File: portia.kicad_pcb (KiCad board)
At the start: 2 copper layers, 65.1 x 56.1 mm, 60 parts, among them J1 USB_B_Micro, J11 Conn_01x02, J12 Conn_01x02, J13 Conn_01x02, J14 Conn_01x02, J2 Conn_02x04_Counter_Clockwise, J3 Conn_01x02, J4 Conn_01x02, J5 RASPBERRYPI-40-PIN-GPIO, J7 Conn_01x02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

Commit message: modified trace connections
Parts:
- removed D8: D, Diode_SMD:D_SOD-123F
- removed JP8, JP9: SolderJumper_2_Open, Jumper:SolderJumper-2_P1.3mm_Open_RoundedPad1.0x1.5mm
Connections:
- J5 pad 1: Net-(D8-Pad1) -> +3V3
- J5 pad 17: Net-(D8-Pad1) -> +3V3
- R15 pad 2: Net-(JP8-Pad2) -> /id_clk
- R16 pad 2: Net-(JP9-Pad2) -> /id_sda
- U6 pad 17: Net-(JP9-Pad2) -> Net-(U6-Pad17)
- U6 pad 18: Net-(JP8-Pad2) -> Net-(U6-Pad18)
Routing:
- net Net-(JP9-Pad2): track 16.3 -> 0.00 mm
- net Net-(D8-Pad1): track 5.24 -> 0.00 mm
- net +5V: track 17.5 -> 12.5 mm
- net /id_sda: track 17.0 -> 21.4 mm
- net +3V3: track 16.8 -> 12.6 mm, vias 2 -> 1
- net GND: track 58.8 -> 54.8 mm, vias 27 -> 26
- net Net-(JP8-Pad2): track 3.46 -> 0.00 mm
- net Net-(F1-Pad1): track 19.7 -> 17.1 mm, vias 3 -> 2
- net /id_clk: track 22.4 -> 23.9 mm
- net Net-(D1-Pad1): track 15.0 -> 15.9 mm
- net Net-(J11-Pad2): track 20.7 -> 20.1 mm

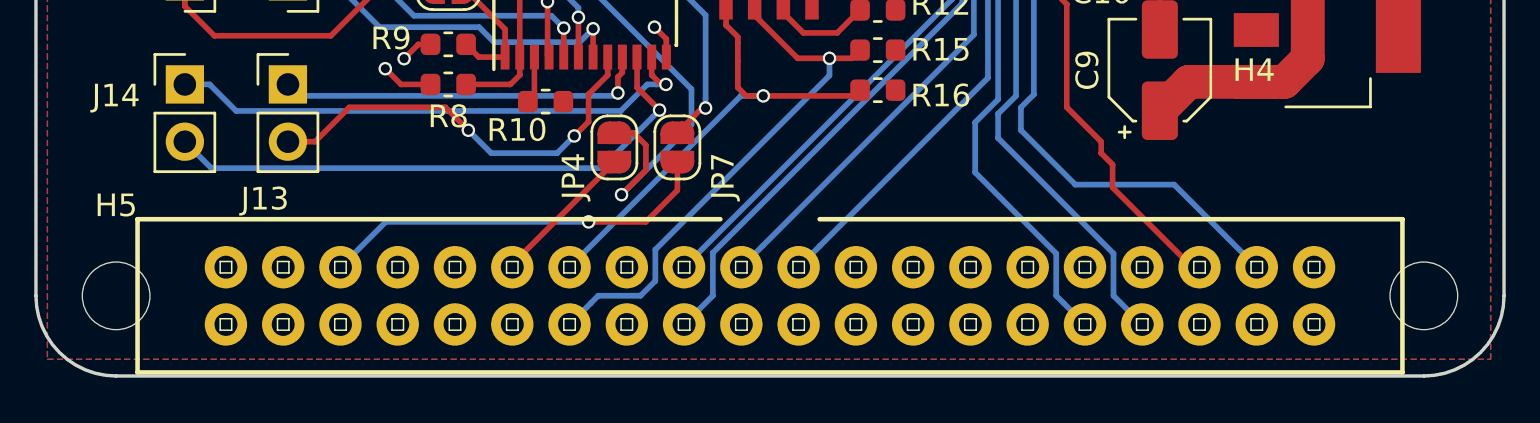
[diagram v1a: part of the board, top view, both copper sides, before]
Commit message: resolved routing issue
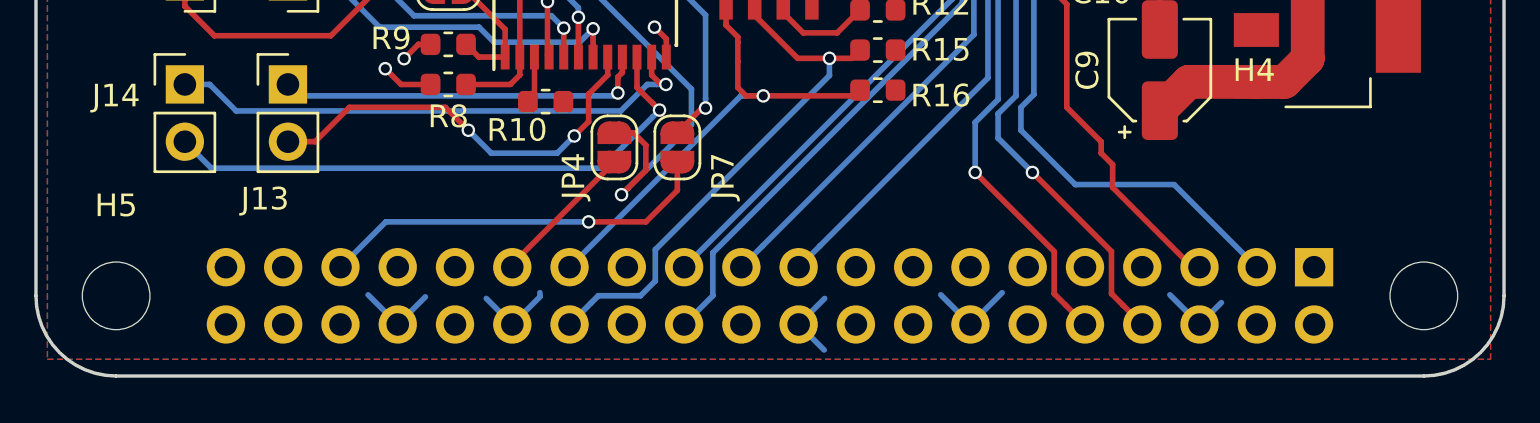
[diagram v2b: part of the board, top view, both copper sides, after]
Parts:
- J5: footprint SparkFun-Boards:2X20-SHROUDED -> Connector_PinSocket_2.54mm:PinSocket_2x20_P2.54mm_Vertical; moved to B.Cu
- moved J5 24.2 mm to (213.2, 129.0), turned to 90 degrees
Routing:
- net GND: track 54.8 -> 72.2 mm
- net /tx: vias 1 -> 2
- net /rx: vias 1 -> 2

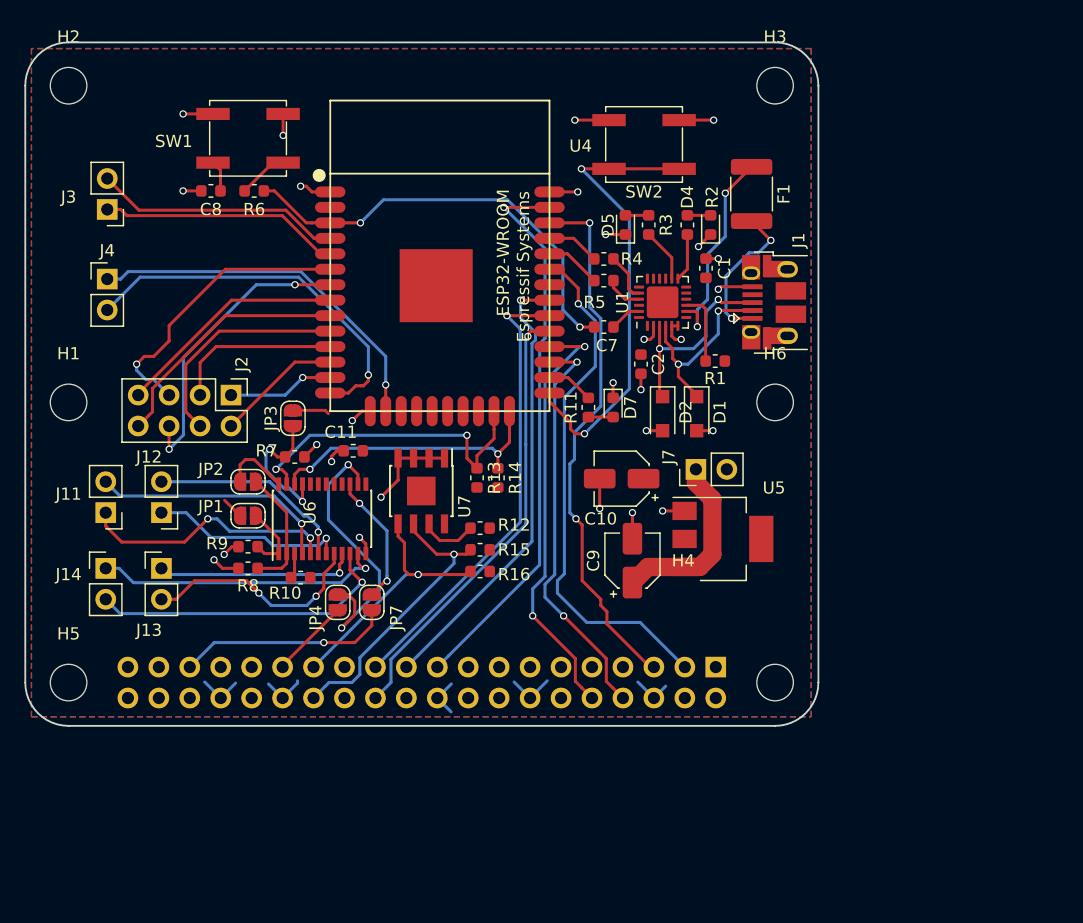
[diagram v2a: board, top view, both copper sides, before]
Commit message: redesign removed 40 pin header
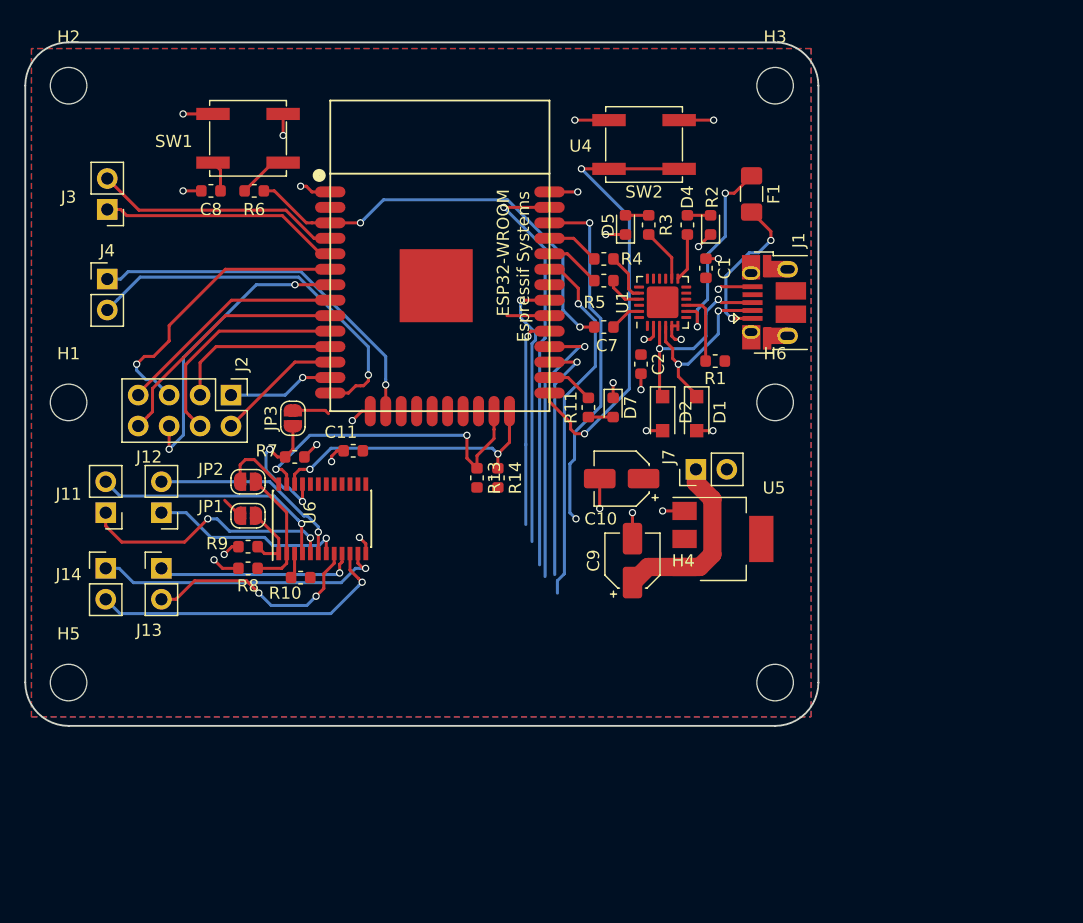
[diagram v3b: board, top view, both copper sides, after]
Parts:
- removed J5: RASPBERRYPI-40-PIN-GPIO, Connector_PinSocket_2.54mm:PinSocket_2x20_P2.54mm_Vertical
- removed JP4, JP7: SolderJumper_2_Open, Jumper:SolderJumper-2_P1.3mm_Open_RoundedPad1.0x1.5mm
- removed R12, R15, R16: R_Small, Resistor_SMD:R_0603_1608Metric
- removed U7: CAT24C256, Package_SO:SOIC-8-1EP_3.9x4.9mm_P1.27mm_EP2.35x2.35mm
- F1: footprint Fuse:Fuse_1812_4532Metric_Pad1.30x3.40mm_HandSolder -> Fuse:Fuse_1206_3216Metric_Pad1.42x1.75mm_HandSolder
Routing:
- net /clk: track 37.7 -> 3.50 mm, vias 1 -> 0
- net GND: track 72.2 -> 47.2 mm, vias 26 -> 25
- net /id_clk: track 23.9 -> 0.00 mm, vias 1 -> 0
- net Net-(U6-Pad14): track 23.3 -> 0.00 mm, vias 2 -> 0
- net /id_sda: track 21.4 -> 0.00 mm, vias 1 -> 0
- net /cs: track 36.9 -> 17.6 mm
- net Net-(J5-Pad35): track 17.6 -> 0.00 mm, vias 1 -> 0
- net /scl0: track 44.2 -> 29.2 mm
- net /miso: track 37.4 -> 22.8 mm
- net /rx: track 33.6 -> 20.5 mm, vias 2 -> 1
- net /sda0: track 42.9 -> 29.9 mm
- net /tx: track 35.8 -> 23.4 mm, vias 2 -> 1
- net /mosi: track 46.6 -> 34.7 mm
- net Net-(U6-Pad15): track 10.9 -> 0.00 mm, vias 2 -> 0
- net Net-(J5-Pad29): track 6.54 -> 0.00 mm
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
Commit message: redesign
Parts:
- removed SW2: Bootloader, Button_Switch_SMD:SW_SPST_EVPBF
- moved J14 28.0 mm to (189.8, 129.3), turned to 270 degrees
- moved J13 17.4 mm to (182.9, 129.3), turned to 270 degrees
- moved J12 14.8 mm to (175.3, 129.0), turned to 270 degrees
- moved J11 13.5 mm to (168.2, 128.8), turned to 270 degrees
- moved J7 12.6 mm to (215.5, 124.7)
- moved JP3 11.4 mm to (168.2, 113.8), turned to 180 degrees
- moved JP2 7.08 mm to (168.2, 116.6)
- moved JP1 7.06 mm to (168.3, 119.4)
- moved R7 7.02 mm to (171.7, 113.0), turned to 90 degrees
- moved R13 6.99 mm to (186.6, 113.5)
- moved R14 6.67 mm to (188.6, 113.5)
- moved C10 5.57 mm to (207.1, 118.8)
- moved C9 5.24 mm to (209.1, 124.7), turned to 180 degrees
- moved U5 1.78 mm to (215.5, 118.8)
- moved C11 1.09 mm to (182.4, 111.8)
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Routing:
- net /mosi: track 34.7 -> 0.00 mm, vias 1 -> 0
- net /sda0: track 29.9 -> 0.00 mm, vias 1 -> 0
- net /scl0: track 29.2 -> 0.00 mm, vias 2 -> 0
- net Net-(J14-Pad2): track 25.4 -> 0.00 mm, vias 1 -> 0
- net Net-(SW2-Pad1): track 37.9 -> 13.7 mm
- net Net-(J14-Pad1): track 23.9 -> 0.00 mm, vias 1 -> 0
- net /tx: track 23.4 -> 0.00 mm, vias 1 -> 0
- net /miso: track 22.8 -> 0.00 mm, vias 1 -> 0
- net Net-(J11-Pad1): track 21.2 -> 0.00 mm, vias 2 -> 0
- net /rx: track 20.5 -> 0.00 mm, vias 1 -> 0
- net Net-(J11-Pad2): track 20.1 -> 0.00 mm, vias 1 -> 0
- net Net-(J13-Pad2): track 18.6 -> 0.00 mm, vias 2 -> 0
- net /cs: track 17.6 -> 0.00 mm, vias 1 -> 0
- net Net-(J12-Pad2): track 16.6 -> 0.00 mm, vias 1 -> 0
- net Net-(J13-Pad1): track 16.6 -> 0.00 mm, vias 1 -> 0
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
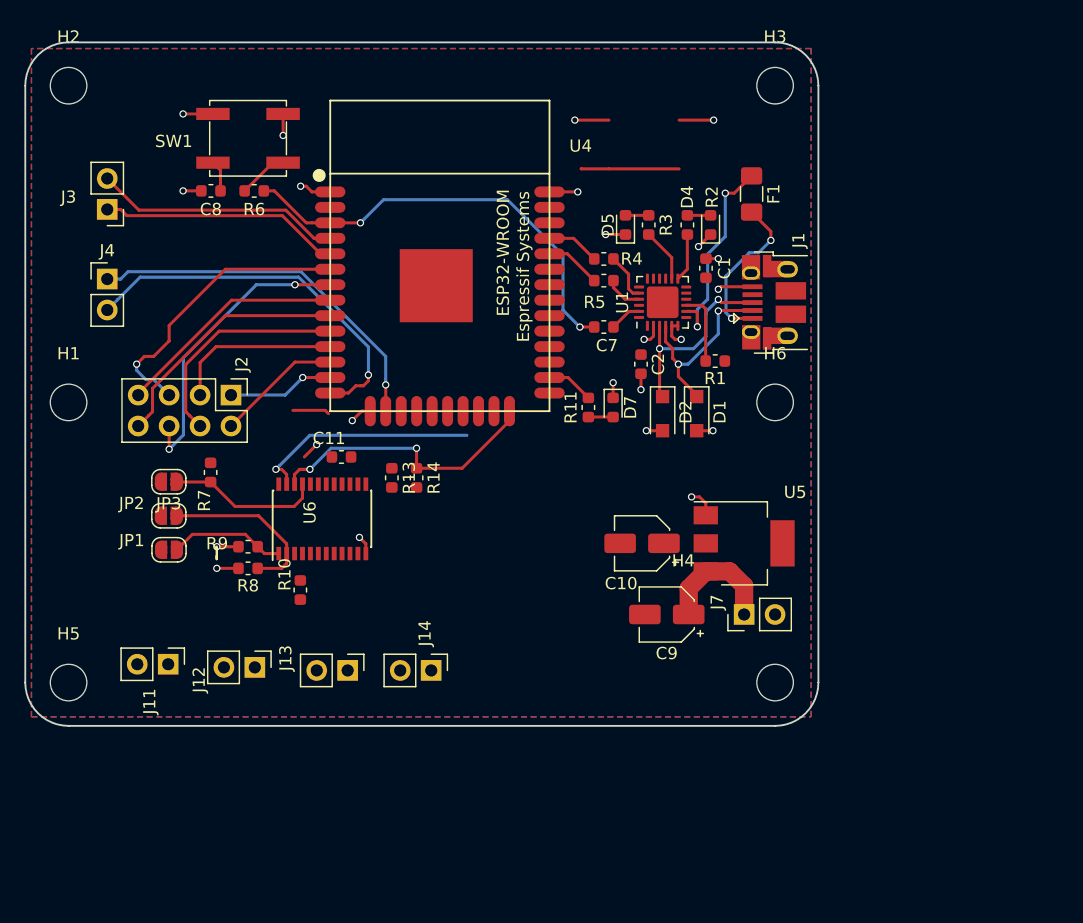
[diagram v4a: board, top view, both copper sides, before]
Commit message: redesigned i2c bus
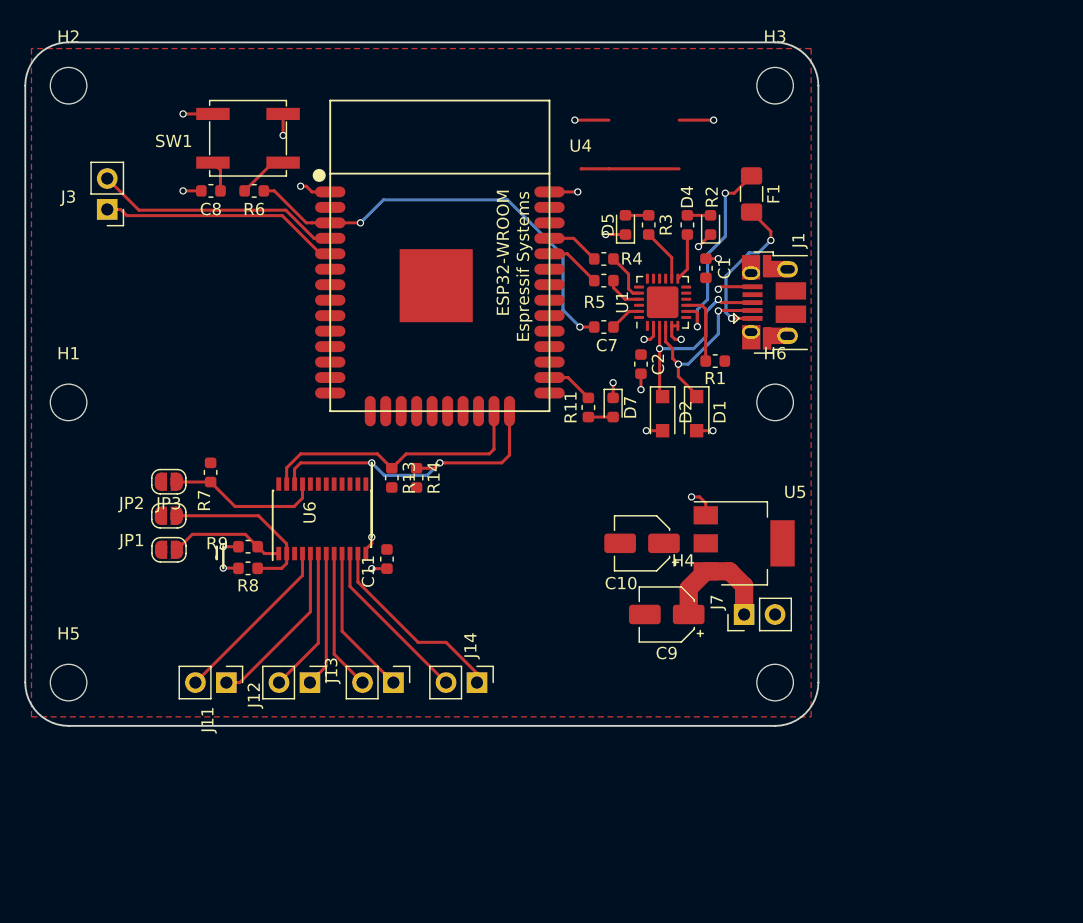
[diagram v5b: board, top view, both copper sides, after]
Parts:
- removed J2: Conn_02x04_Counter_Clockwise, Connector_PinHeader_2.54mm:PinHeader_2x04_P2.54mm_Vertical
- removed J4: Conn_01x02, Connector_PinHeader_2.54mm:PinHeader_1x02_P2.54mm_Vertical
- removed R10: R_Small, Resistor_SMD:R_0603_1608Metric
- moved C11 9.18 mm to (186.2, 120.1), turned to 270 degrees
- moved J11 5.01 mm to (173.0, 130.3)
- moved J12 4.69 mm to (179.8, 130.3)
- moved J14 3.89 mm to (193.5, 130.3)
- moved J13 3.89 mm to (186.7, 130.3)
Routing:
- net Net-(J4-Pad2): track 31.4 -> 0.00 mm, vias 1 -> 0
- net Net-(J4-Pad1): track 30.5 -> 0.00 mm, vias 1 -> 0
- net Net-(J2-Pad6): track 25.5 -> 1.04 mm, vias 2 -> 0
- net Net-(J2-Pad5): track 23.9 -> 0.00 mm, vias 1 -> 0
- net Net-(J2-Pad8): track 20.6 -> 0.00 mm
- net Net-(J2-Pad7): track 19.1 -> 0.00 mm
- net Net-(J2-Pad4): track 18.5 -> 0.00 mm
- net Net-(J14-Pad1): track 0.00 -> 16.0 mm
- net Net-(J11-Pad2): track 0.00 -> 14.2 mm
- net Net-(J11-Pad1): track 0.00 -> 14.1 mm
- net Net-(J2-Pad3): track 13.9 -> 0.00 mm
- net Net-(J14-Pad2): track 0.00 -> 13.9 mm
- net Net-(J13-Pad1): track 0.00 -> 12.3 mm
- net Net-(J12-Pad2): track 0.00 -> 11.9 mm
- net Net-(J13-Pad2): track 0.00 -> 11.6 mm
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- removed copper zone on B.Cu, net GND

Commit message: removed extra trace
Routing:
- net Net-(SW2-Pad1): track 13.7 -> 0.00 mm, vias 2 -> 0
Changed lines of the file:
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@@
     (thickness 1.6)
     (drawings 12)
-    (tracks 262)
+    (tracks 254)
     (zones 0)
     (modules 46)
@@
   (segment (start 201.0235 105.24) (end 202.692 106.9085) (width 0.25) (layer F.Cu) (net 45))
   (segment (start 199.5 105.24) (end 201.0235 105.24) (width 0.25) (layer F.Cu) (net 45))
-  (segment (start 210.144 84.106) (end 212.979 84.106) (width 0.25) (layer F.Cu) (net 46))
-  (via (at 212.979 84.106) (size 0.6) (drill 0.4) (layers F.Cu B.Cu) (net 46))
-  (segment (start 204.384 84.106) (end 201.5805 84.106) (width 0.25) (layer F.Cu) (net 46))
-  (segment (start 201.5805 84.106) (end 201.5805 84.106) (width 0.25) (layer F.Cu) (net 46))
-  (via (at 201.5805 84.106) (size 0.6) (drill 0.4) (layers F.Cu B.Cu) (net 46))
-  (segment (start 204.384 88.106) (end 202.1205 88.106) (width 0.25) (layer F.Cu) (net 46))
-  (segment (start 202.1205 88.106) (end 202.089 88.106) (width 0.25) (layer F.Cu) (net 46))
-  (segment (start 204.384 88.106) (end 210.144 88.106) (width 0.25) (layer F.Cu) (net 46))
   (segment (start 179.07 112.246) (end 184.912 112.246) (width 0.25) (layer F.Cu) (net 77))
   (segment (start 178.573 112.743) (end 179.07 112.246) (width 0.25) (layer F.Cu) (net 77))
